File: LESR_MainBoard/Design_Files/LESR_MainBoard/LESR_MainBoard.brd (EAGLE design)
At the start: 79.2 x 38.4 mm, 39 parts, among them J1 DCJ0202, Q1 SS8050-G, Q2 SS8050-G, U1 TCA9548APWR, U2 NCP1117ST33T3G, U3 ESP32-WROOM-32, U4 CP2102N-A01-GQFN28, U5 SP0503BAHT

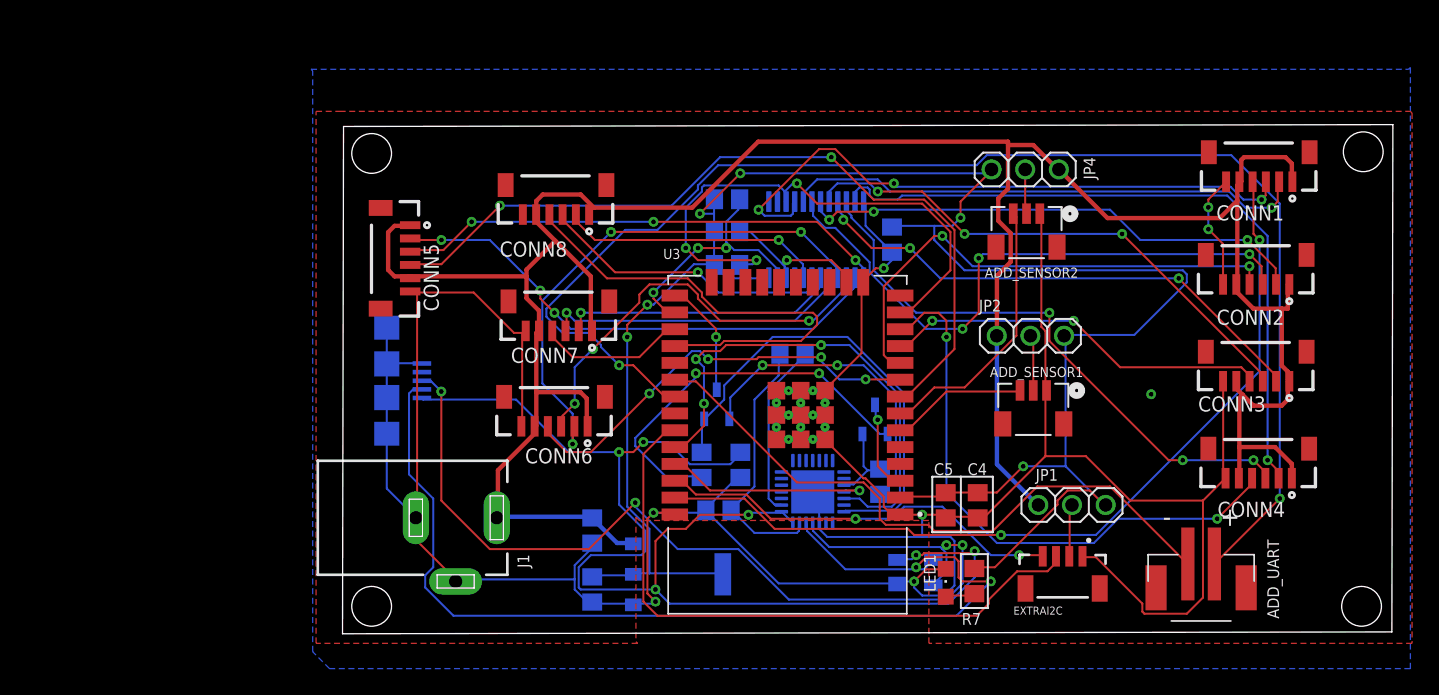
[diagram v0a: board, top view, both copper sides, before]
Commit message: 12V to 5V LDO version
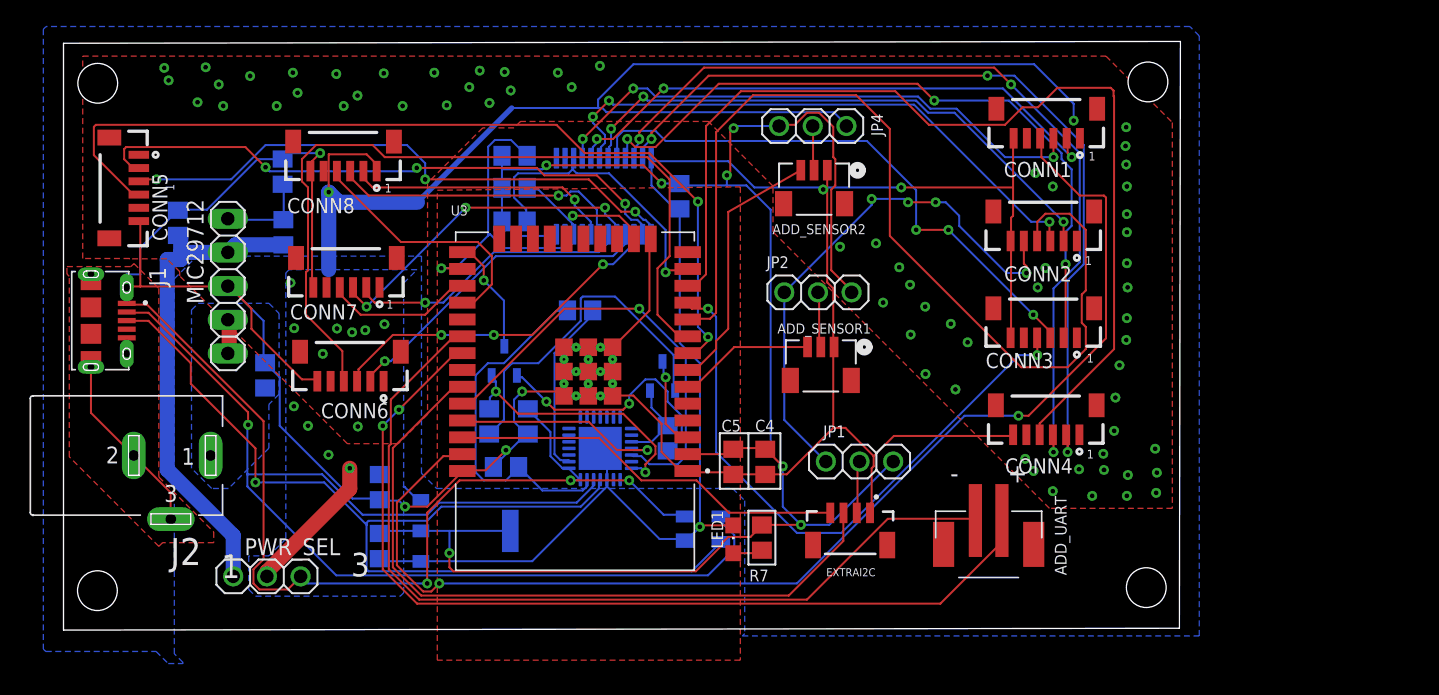
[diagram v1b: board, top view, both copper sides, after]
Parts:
- removed USB: (no value), SparkFun-Connectors:USB-MICROB
- added C8, C9: 10uF, rcl:C0805
- added J2: 694106301002, DC Power Jacks:694106301002
- added MIC29712: 12V to 5V 7.5A LDO, pinhead:1X05
- added PWR_SEL: (no value), adafruit:1X03
- added R8: 4.7k, rcl:R0805
- added R9: 1.5k, rcl:R0805
- C6: value 1uF -> 4.7uF
- J1: value DCJ0202 -> 10118194-0001LF; device con-jack:DCJ0202 -> ThHole-USB-Micro-BType-receptacle:AMPHENOL_10118194-0001LF
- moved J1 31.3 mm to (2.07, 23.3)
- moved CONN5 21.1 mm to (4.41, 33.3)
- moved ADD_SENSOR2 16.4 mm to (56.6, 33.2)
- moved EXTRAI2C 16.4 mm to (59.4, 9.60)
- moved ADD_SENSOR1 16.4 mm to (57.1, 19.9)
- moved ADD_UART 16.4 mm to (69.8, 6.45)
- moved C1 16.4 mm to (23.9, 10.8)
- moved C2 16.4 mm to (23.9, 6.32)
- moved C3 16.4 mm to (46.5, 32.7)
- moved C4 16.4 mm to (52.9, 12.7)
- moved C5 16.4 mm to (50.5, 12.7)
- moved C6 16.4 mm to (35.0, 15.7)
- moved C7 16.4 mm to (33.4, 12.3)
- moved CONN1 16.4 mm to (74.1, 38.4)
- moved CONN2 16.4 mm to (73.9, 30.6)
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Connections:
- new net DC_IN: C9.1, J2.1, MIC29712.1, MIC29712.2
- new net LDO_5V: C8.1, MIC29712.4, PWR_SEL.1, R8.2
- new net N$2: MIC29712.5, R8.1, R9.2
- net DN: now also J1.2; no longer USB.D-
- net DP: now also J1.3; no longer USB.D+
- net GND: now also C8.2, C9.2, J1.5, J1.S1, J1.S2, J1.S3, J1.S4, J1.S5, J1.S6, J2.2, J2.3, MIC29712.3, R9.1; no longer J1.2, J1.3, USB.GND, USB.MT1, USB.MT2, USB.P$1, USB.P$2
- net VBUS: now also J1.1, PWR_SEL.3; no longer USB.VBUS
- net VIN: now also PWR_SEL.2; no longer J1.1
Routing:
- net VIN: track 204.6 -> 149.5 mm, vias 0 -> 9
- net GND: track 267.1 -> 309.9 mm, vias 8 -> 7
- net LDO_5V: track 0.00 -> 36.9 mm
- net IO25: track 38.2 -> 73.9 mm, vias 2 -> 0
- net E_RX: track 103.9 -> 70.5 mm
- net IO27: track 44.1 -> 75.4 mm, vias 2 -> 0
- net IO33: track 32.0 -> 61.0 mm, vias 4 -> 0
- net IO23: track 64.9 -> 91.7 mm
- net VBUS: track 97.1 -> 75.5 mm, vias 6 -> 3
- net SD3: track 43.6 -> 64.7 mm
- net E_TX: track 48.1 -> 68.0 mm
- net M_RST: track 42.6 -> 23.1 mm, vias 3 -> 1
- net IO26: track 29.3 -> 46.5 mm
- net IO17: track 35.9 -> 19.6 mm
- net DTR: track 35.6 -> 20.1 mm, vias 0 -> 2
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- added copper zone on layer 16, net DC_IN
- added copper zone on layer 1, net VIN
- added copper zone on layer 16, net VIN
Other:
- board size 79.2 x 38.4 mm -> 84.3 x 44.4 mm
- board text added: "1"
- board text added: "3"
- board text added: "5V"
- board text added: "6"
- board text added: "DIN"
- board text added: "GND"
- board text added: "SCL"
- board text added: "SDA"

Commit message: Controller dimensions changed
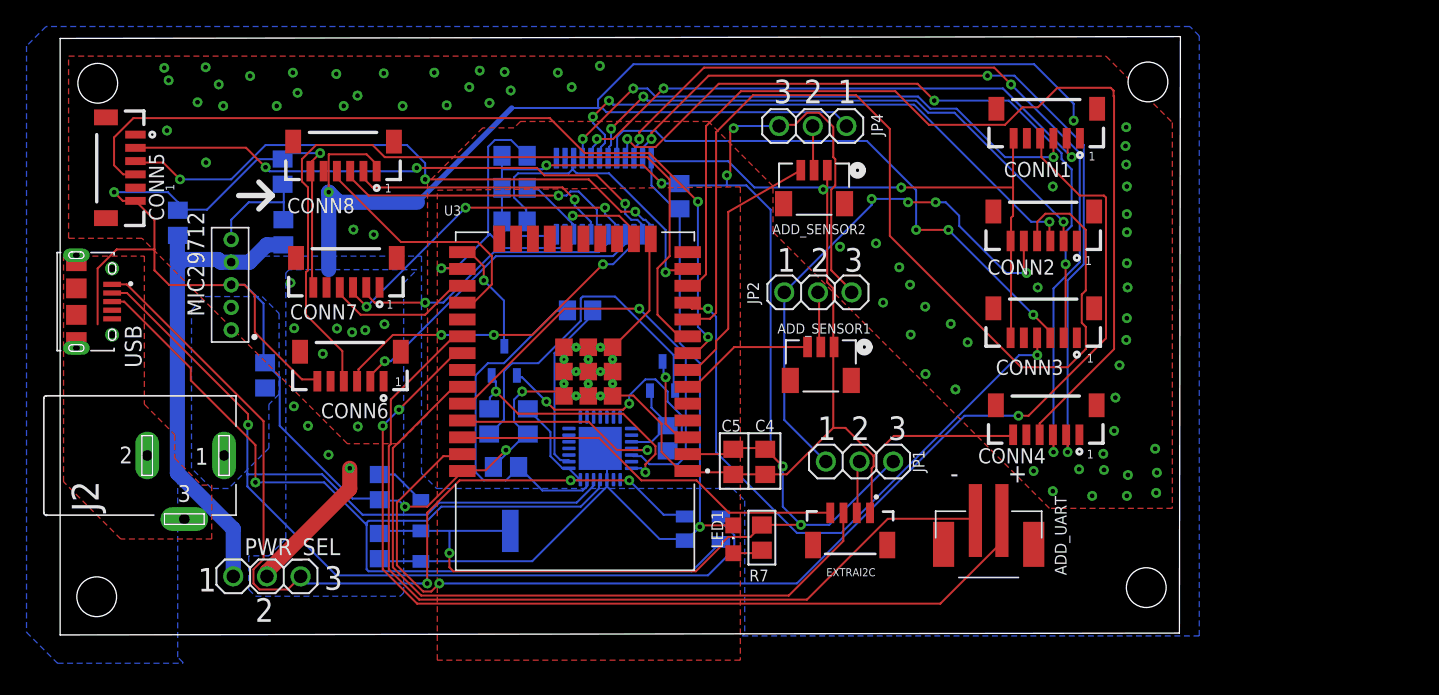
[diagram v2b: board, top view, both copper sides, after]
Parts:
- removed J1: 10118194-0001LF, ThHole-USB-Micro-BType-receptacle:AMPHENOL_10118194-0001LF
- added USB: 10118194-0001LF, ThHole-USB-Micro-BType-receptacle:AMPHENOL_10118194-0001LF
- MIC29712: value 12V to 5V 7.5A LDO -> MIC29712WT; device pinhead:1X05 -> MIC29712WT:TO170P1066X482X1572-5
- moved MIC29712 3.31 mm to (12.6, 22.6)
- moved CONN5 1.55 mm to (4.15, 34.8)
- moved J2 1.02 mm to (-1.49, 13.2)
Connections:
- net DN: now also USB.2; no longer J1.2
- net DP: now also USB.3; no longer J1.3
- net GND: now also USB.5, USB.S1, USB.S2, USB.S3, USB.S4, USB.S5, USB.S6; no longer J1.5, J1.S1, J1.S2, J1.S3, J1.S4, J1.S5, J1.S6
- net VBUS: now also USB.1; no longer J1.1
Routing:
- net GND: track 309.9 -> 305.3 mm, vias 7 -> 8
- net IO32: track 67.5 -> 64.0 mm
- net SC4: track 45.2 -> 42.1 mm
- net DC_IN: track 2.68 -> 0.00 mm
- net VIN: track 149.5 -> 151.7 mm
- net N$2: track 6.92 -> 8.72 mm
- net VBUS: track 75.5 -> 77.1 mm
- net DN: track 89.9 -> 91.5 mm
- net DP: track 77.4 -> 78.9 mm
- net LDO_5V: track 36.9 -> 36.1 mm
- net SD4: track 43.7 -> 44.5 mm
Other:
- board size 84.3 x 44.4 mm -> 84.5 x 45.1 mm
- board text added: "1 & 2"
- board text added: "2"
- board text added: "2 & 3"
- board text added: "3.3V"
- board text added: "Closed"
- board text added: "DC_Jack/"
- board text added: "USB/"
